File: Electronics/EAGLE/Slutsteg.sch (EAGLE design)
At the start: 151 parts, among them CN1 OSTYK33102030-2, CN2 OSTYK33102030-2, CN3 OSTYK33102030-2, IC1 SPX1117M3-L-3-3_TR, IC10 LM324D, IC11 L78M12ABDT-TR, IC3 ESP32-WROVER-IE-4MB, IC4 TM8211, IC6 TPA3244DDWR, IC7 TPA3251D2DDVR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

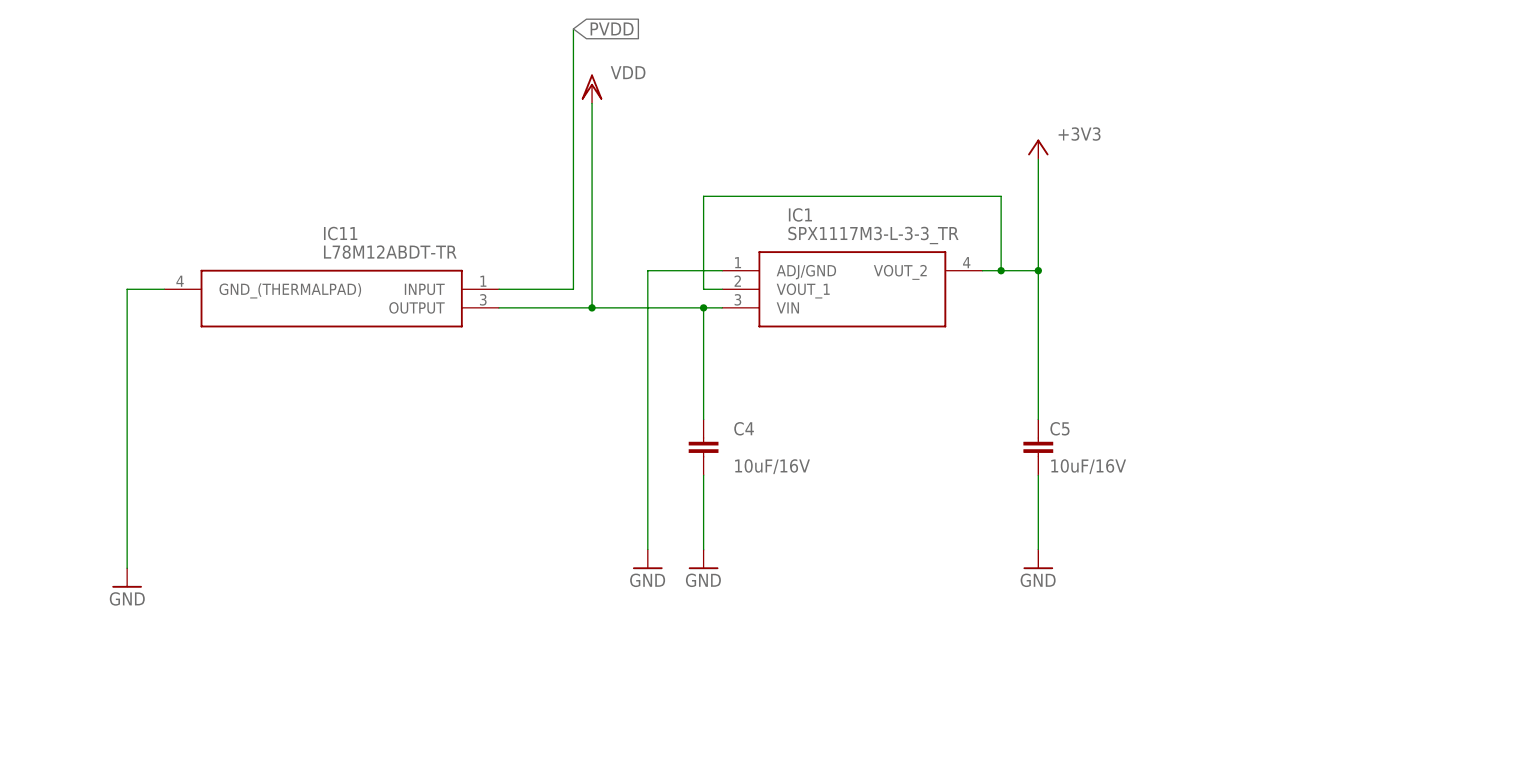
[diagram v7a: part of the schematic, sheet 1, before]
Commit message: ALmost done with the ESP32 & TPA3244 layout
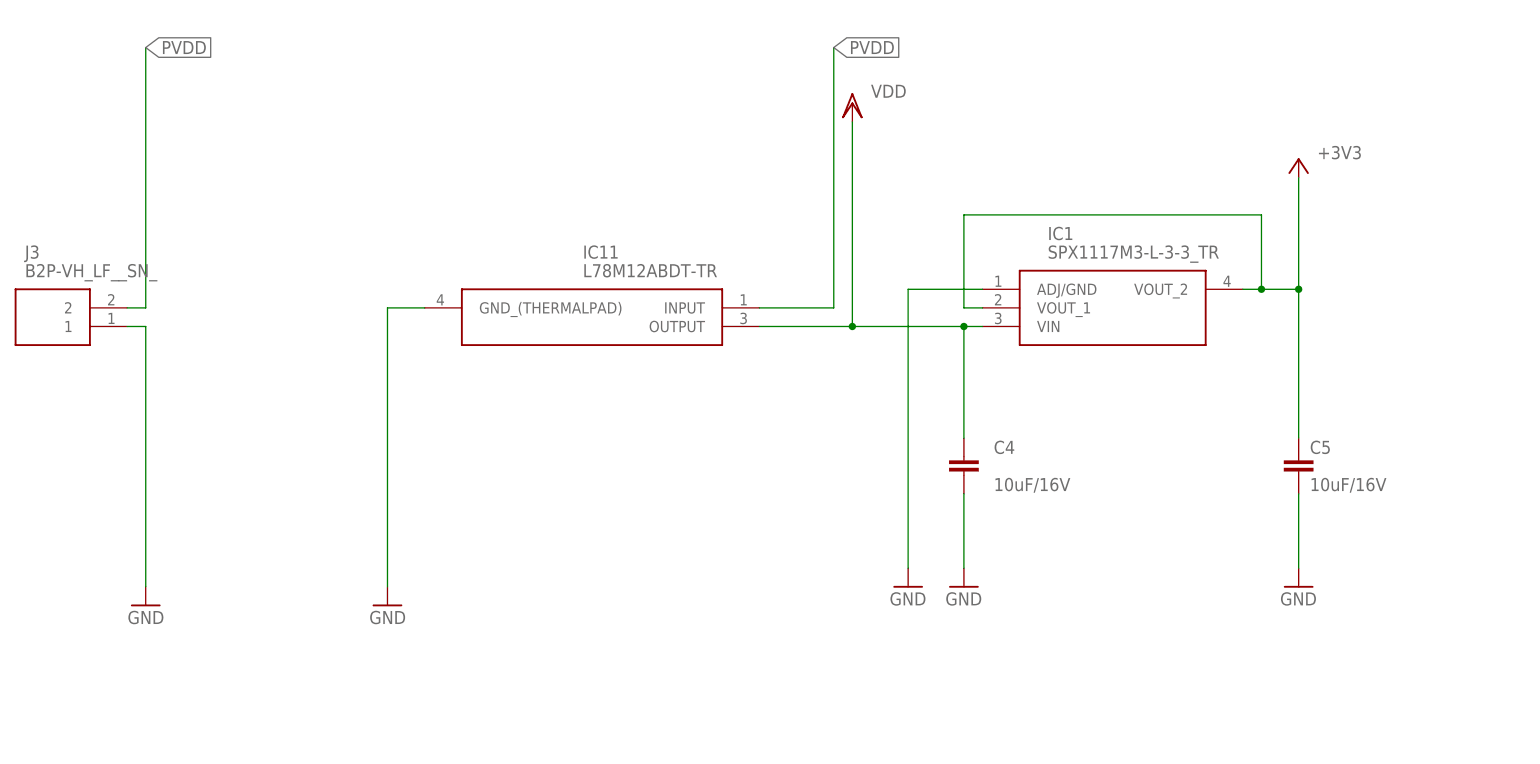
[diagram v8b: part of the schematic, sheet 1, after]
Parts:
- added J3: B2P-VH_LF__SN_, SamacSys_Parts:B2P-VH_LF__SN_
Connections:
- net GND: now also J3.1
- net PVDD: now also J3.2
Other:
- moved on the sheet: C4, C5, IC1, IC11
